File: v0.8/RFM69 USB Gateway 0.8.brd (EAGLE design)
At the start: 40.7 x 17.3 mm, 25 parts, among them CN1 MINIB, IC3 MCP1703CB, U2 ATMEGA328P-MU, X1 16 MHz

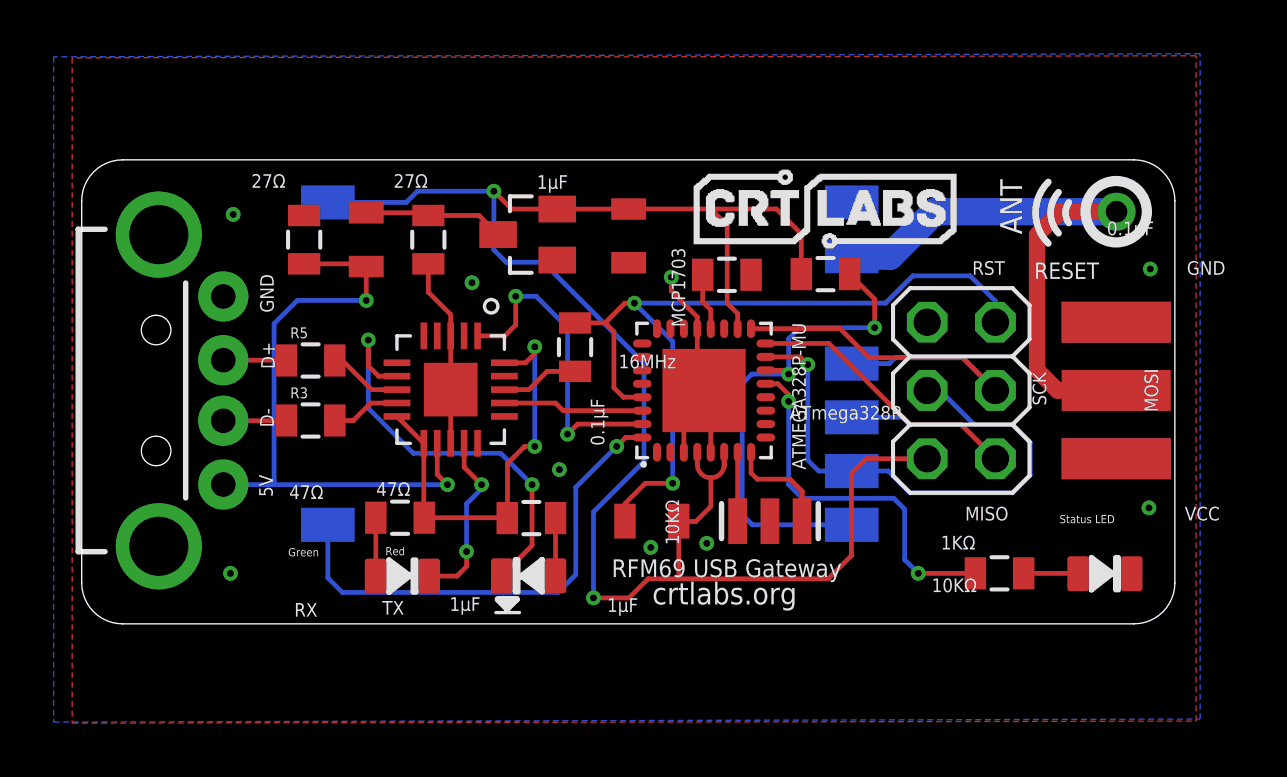
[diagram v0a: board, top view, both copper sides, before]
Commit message: Unsmashed and updated all component values
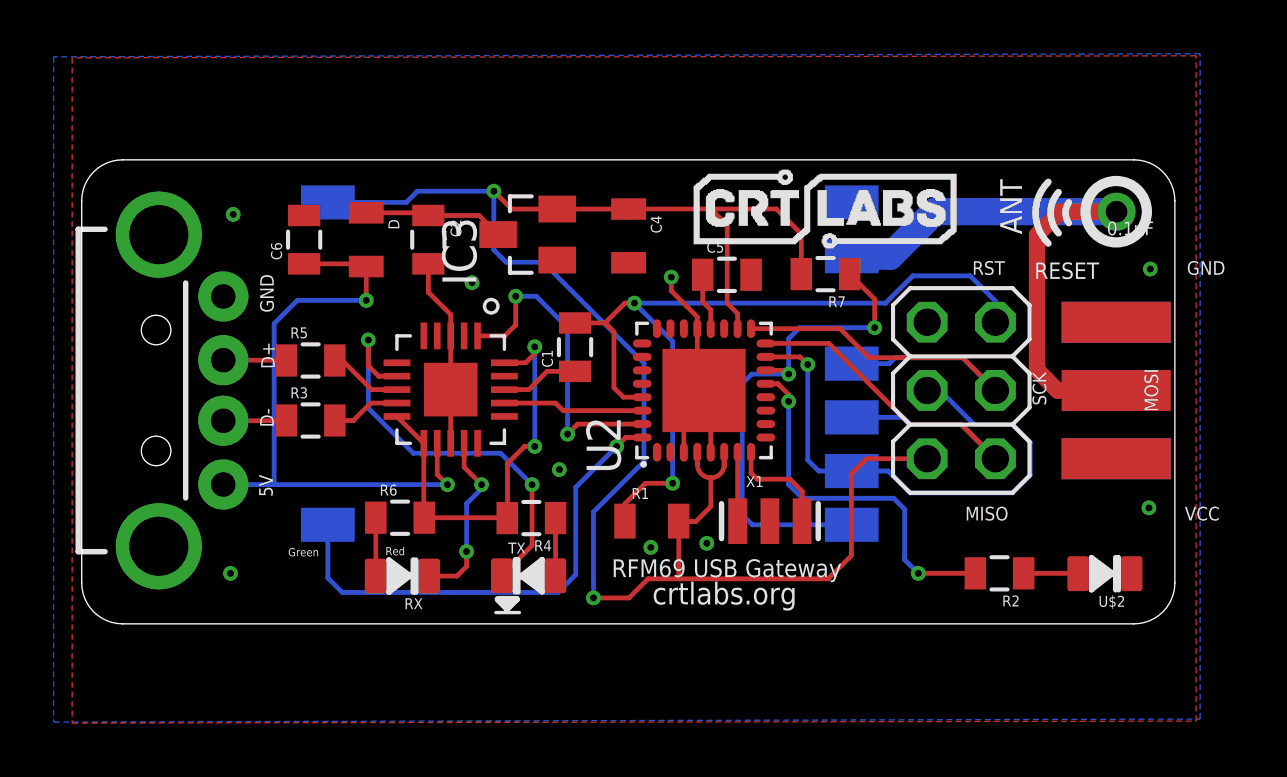
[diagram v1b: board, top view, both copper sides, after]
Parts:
- C1, C5: value 0.1 -> 0.1μF
- C2, C4: value 1u -> 1μF
- C6: value 0.1u -> 0.1μF
- R1: value 10k -> 10KΩ
- R2: value 1k -> 1KΩ
- R4, R6: value (none) -> 47Ω
- R7: value 10K -> 10KΩ
- RX: value LED0805 -> Green
- TX: value LED0805 -> Red
- renumbered U$4 to RX, U$7 to TX
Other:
- board text removed: "10KΩ"
- board text removed: "16MHz"
- board text removed: "1KΩ"
- board text removed: "1μF"
- board text removed: "27Ω"
- board text removed: "47Ω"
- board text removed: "ATmega328P"
- board text removed: "MCP1703"
- board text removed: "RX"
- board text removed: "Status LED"
- board text removed: "TX"
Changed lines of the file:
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@@
 <text x="51.6382" y="4.0894" size="1.016" layer="22" font="vector" ratio="15" rot="MR0">Akram Ali</text>
 <text x="13.462" y="11.5697" size="0.8128" layer="22" font="vector" ratio="9" rot="MR270" align="bottom-center">v0.8    2016</text>
-<text x="18.4023" y="19.1262" size="0.508" layer="121" font="vector">27Ω</text>
-<text x="23.6982" y="19.1262" size="0.508" layer="121" font="vector">27Ω</text>
-<text x="19.812" y="7.5438" size="0.508" layer="121" font="vector">47Ω</text>
-<text x="23.0505" y="7.6581" size="0.508" layer="121" font="vector">47Ω</text>
-<text x="34.3281" y="5.8293" size="0.508" layer="121" font="vector" rot="R90">10KΩ</text>
-<text x="44.069" y="5.6642" size="0.508" layer="121" font="vector">1KΩ</text>
-<text x="26.9367" y="3.8862" size="0.508" layer="121" font="vector" rot="R180">1μF</text>
-<text x="32.8041" y="3.8481" size="0.508" layer="121" font="vector" rot="R180">1μF</text>
 <text x="52.0065" y="17.8689" size="0.508" layer="121" font="vector" rot="R180">0.1μF</text>
-<text x="29.0322" y="19.0881" size="0.508" layer="121" font="vector">1μF</text>
-<text x="20.0025" y="3.1623" size="0.508" layer="121" font="vector">RX</text>
-<text x="23.2791" y="3.2385" size="0.508" layer="121" font="vector">TX</text>
 <text x="19.7739" y="5.4102" size="0.3048" layer="121" font="vector">Green</text>
 <text x="23.3934" y="5.4483" size="0.3048" layer="121" font="vector">Red</text>
-<text x="34.2138" y="12.9159" size="0.508" layer="121" font="vector" rot="R180">16MHz</text>
-<text x="34.5567" y="13.9446" size="0.508" layer="121" font="vector" rot="R90">MCP1703</text>
-<text x="48.4886" y="6.6421" size="0.3048" layer="121" font="vector">Status LED</text>
 <text x="19.2405" y="14.478" size="0.508" layer="121" font="vector" rot="R90">GND</text>
 <text x="19.2786" y="12.3825" size="0.508" layer="121" font="vector" rot="R90">D+</text>
@@
 <text x="31.8135" y="4.6355" size="0.6604" layer="21" font="vector" ratio="7">RFM69 USB Gateway</text>
 <text x="33.3248" y="3.6195" size="0.8128" layer="21" font="vector" ratio="12">crtlabs.org</text>
-<text x="43.7261" y="4.0767" size="0.508" layer="121" font="vector">10KΩ</text>
 <text x="46.2788" y="19.4437" size="0.8128" layer="21" font="vector" rot="R270">ANT</text>
-<text x="42.5958" y="11.0109" size="0.508" layer="121" font="vector" rot="R180">ATmega328P</text>
-<text x="31.5468" y="9.525" size="0.508" layer="121" font="vector" rot="R90">0.1μF</text>
 <rectangle x1="39.78275" y1="16.87195" x2="40.08755" y2="16.91005" layer="121"/>
 <rectangle x1="39.70655" y1="16.91005" x2="40.12565" y2="16.94815" layer="121"/>
@@
 </autorouter>
 <elements>
-<element name="X1" library="SparkFun" package="RESONATOR-SMD" value="16 MHz" x="37.7063" y="6.7183" smashed="yes"/>
-<element name="IC3" library="linear" package="SOT23" value="MCP1703CB" x="28.6893" y="17.3863" smashed="yes" rot="R90"/>
-<element name="C5" library="SparkFun" package="0805" value="0.1" x="36.1061" y="15.8877" smashed="yes"/>
-<element name="R1" library="LowPowerLab" package="0805" value="10k" x="33.3121" y="6.7183" smashed="yes"/>
-<element name="C4" library="LowPowerLab" package="0805" value="1u" x="32.4485" y="17.3355" smashed="yes" rot="R270"/>
-<element name="C2" library="SparkFun" package="0805" value="1u" x="24.9936" y="17.1958" smashed="yes" rot="R270"/>
-<element name="U$2" library="LowPowerLab" package="0805-LED" value="LED0805" x="50.1777" y="4.7625" smashed="yes" rot="R180"/>
-<element name="R2" library="SparkFun" package="0805" value="1k" x="46.2534" y="4.7752" smashed="yes" rot="R180"/>
+<element name="X1" library="SparkFun" package="RESONATOR-SMD" value="16 MHz" x="37.7063" y="6.7183"/>
+<element name="IC3" library="linear" package="SOT23" value="MCP1703CB" x="28.6893" y="17.3863" rot="R90"/>
+<element name="C5" library="SparkFun" package="0805" value="0.1μF" x="36.1061" y="15.8877"/>
+<element name="R1" library="LowPowerLab" package="0805" value="10KΩ" x="33.3121" y="6.7183"/>
+<element name="C4" library="LowPowerLab" package="0805" value="1μF" x="32.4485" y="17.3355" rot="R270"/>
+<element name="C2" library="SparkFun" package="0805" value="1μF" x="24.9936" y="17.1958" rot="R270"/>
+<element name="U$2" library="LowPowerLab" package="0805-LED" value="LED0805" x="50.1777" y="4.7625" rot="R180"/>
+<element name="R2" library="SparkFun" package="0805" value="1KΩ" x="46.2534" y="4.7752" rot="R180"/>
 <element name="U$1" library="LowPowerLab" package="RFM12B-ANTENNA" value="RFM12B_ANTENNA" x="50.6095" y="18.2372"/>
 <element name="U$5" library="LowPowerLab" package="RFM69W-MINPADS" value="RFM69" x="32.7533" y="11.5824" smashed="yes" rot="MR180"/>
@@
 <attribute name="PROD_ID" value="CONN-08367" x="14.9606" y="11.5824" size="1.778" layer="27" display="off"/>
 </element>
-<element name="R4" library="SparkFun" package="0805" value="" x="28.829" y="6.8326" smashed="yes" rot="R180">
-<attribute name="VALUE" x="29.845" y="7.9756" size="0.4064" layer="27" font="vector" rot="R180"/>
-</element>
-<element name="R6" library="SparkFun" package="0805" value="" x="23.9395" y="6.8453" smashed="yes">
-<attribute name="VALUE" x="22.9235" y="5.7023" size="0.4064" layer="27" font="vector"/>
-</element>
-<element name="U$4" library="LowPowerLab" package="0805-LED" value="LED0805" x="24.0284" y="4.6736" smashed="yes" rot="R180"/>
-<element name="U$7" library="LowPowerLab" package="0805-LED" value="LED0805" x="28.7274" y="4.6863" smashed="yes"/>
-<element name="C6" library="SparkFun" package="0805" value="0.1u" x="20.3708" y="17.1958" smashed="yes" rot="R90"/>
-<element name="D" library="LowPowerLab" package="0805" value="SHOTTKY" x="22.6822" y="17.1958" smashed="yes" rot="R270"/>
+<element name="R4" library="SparkFun" package="0805" value="47Ω" x="28.829" y="6.8326" rot="R180"/>
+<element name="R6" library="SparkFun" package="0805" value="47Ω" x="23.9395" y="6.8453"/>
+<element name="RX" library="LowPowerLab" package="0805-LED" value="Green" x="24.0284" y="4.6736" rot="R180"/>
+<element name="TX" library="LowPowerLab" package="0805-LED" value="Red" x="28.7274" y="4.6863"/>
+<element name="C6" library="SparkFun" package="0805" value="0.1μF" x="20.3708" y="17.1958" rot="R90"/>
+<element name="D" library="LowPowerLab" package="0805" value="SHOTTKY" x="22.6822" y="17.1958" rot="R270"/>
 <element name="R3" library="SparkFun" package="0805" value="27Ω" x="20.6121" y="10.4648"/>
 <element name="R5" library="SparkFun" package="0805" value="27Ω" x="20.6121" y="12.7"/>
@@
 <attribute name="VALUE" x="49.276" y="7.7724" size="1.27" layer="27" rot="R90"/>
 </element>
-<element name="R7" library="SparkFun" package="0805" value="10K" x="39.7764" y="15.9131" smashed="yes" rot="R180"/>
-<element name="C1" library="SparkFun" package="0805" value="0.1" x="30.4546" y="13.1953" smashed="yes" rot="R90"/>
+<element name="R7" library="SparkFun" package="0805" value="10KΩ" x="39.7764" y="15.9131" rot="R180"/>
+<element name="C1" library="SparkFun" package="0805" value="0.1μF" x="30.4546" y="13.1953" rot="R90"/>
 <element name="J$1" library="SparkFun-Connectors" package="SMA-EDGE" value="SMA_EDGE" x="50.5968" y="9.0424" rot="R90"/>
-<element name="U2" library="ATMEGA328P-MU" package="QFN50P500X500X100-33N" value="ATMEGA328P-MU" x="35.2552" y="11.5824" smashed="yes" rot="R90">
+<element name="U2" library="ATMEGA328P-MU" package="QFN50P500X500X100-33N" value="ATMEGA328P-MU" x="35.2552" y="11.5824" rot="R90">
 <attribute name="AVAILABILITY" value="Good" x="35.2552" y="11.5824" size="1.778" layer="27" rot="R90" display="off"/>
 <attribute name="MP" value="ATMEGA328P-MU" x="35.2552" y="11.5824" size="1.778" layer="27" rot="R90" display="off"/>
@@
 <attribute name="MF" value="Atmel" x="35.2552" y="11.5824" size="1.778" layer="27" rot="R90" display="off"/>
 <attribute name="PRICE" value="2.55 USD" x="35.2552" y="11.5824" size="1.778" layer="27" rot="R90" display="off"/>
-<attribute name="VALUE" x="39.043709375" y="8.635590625" size="0.508" layer="121" font="vector" rot="R90"/>
 </element>
 <element name="FT231XQ-R" library="ftdi_ft231xq-r" package="FTDI_FT231XQ-R_PACKAGE" value="FT231XQ-R" x="25.8572" y="11.5824" rot="R270"/>
@@
 </signal>
 <signal name="N$6">
-<contactref element="U$4" pad="MINUS"/>
+<contactref element="RX" pad="MINUS"/>
 <contactref element="FT231XQ-R" pad="CBUS1"/>
 <wire x1="26.3252" y1="9.6144" x2="26.3252" y2="8.7268" width="0.1778" layer="1"/>
@@
 </signal>
 <signal name="N$7">
-<contactref element="U$7" pad="MINUS"/>
+<contactref element="TX" pad="MINUS"/>
 <contactref element="FT231XQ-R" pad="CBUS2"/>
 <wire x1="23.8252" y1="12.1144" x2="23.1408" y2="12.1144" width="0.1778" layer="1"/>
@@
 <signal name="N$8">
 <contactref element="R4" pad="1"/>
-<contactref element="U$7" pad="PLUS"/>
+<contactref element="TX" pad="PLUS"/>
 <wire x1="29.7274" y1="4.6863" x2="29.7274" y2="6.831" width="0.1778" layer="1"/>
 <wire x1="29.7274" y1="6.831" x2="29.729" y2="6.8326" width="0.1778" layer="1"/>
 </signal>
 <signal name="N$9">
-<contactref element="U$4" pad="PLUS"/>
+<contactref element="RX" pad="PLUS"/>
 <contactref element="R6" pad="1"/>
 <wire x1="23.0395" y1="6.8453" x2="23.0395" y2="4.6847" width="0.1778" layer="1"/>

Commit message: Fixed silkscreen
Changed all fonts to vector; silkscreen now on layer 121, adjusted some
components and traces
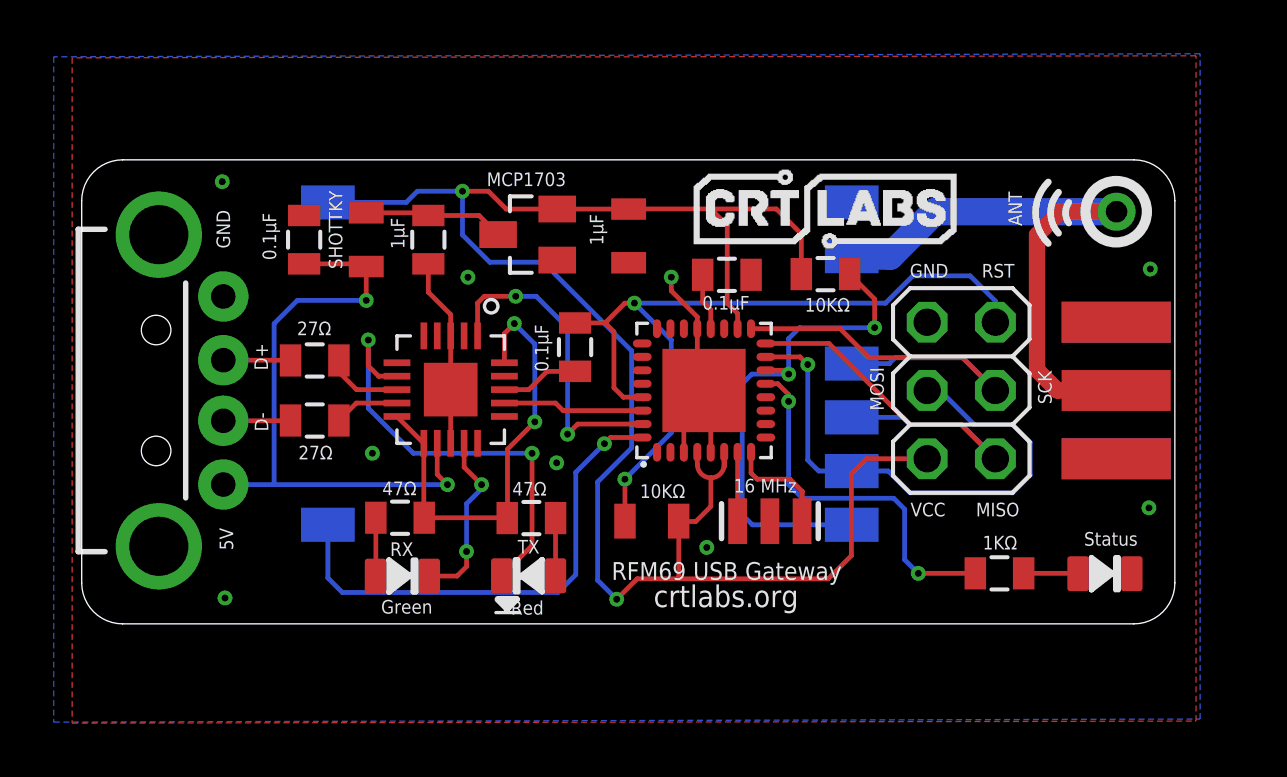
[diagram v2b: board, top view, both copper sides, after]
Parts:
- IC3: value MCP1703CB -> MCP1703
- U$2: value LED0805 -> Status
- moved R3 0.15 mm to (20.8, 10.5)
- moved R5 0.15 mm to (20.8, 12.7)
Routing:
- net FTDI3.3V: track 15.8 -> 16.9 mm
- net N$7: track 15.9 -> 16.5 mm
- net RESET: track 31.3 -> 30.7 mm
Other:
- board text removed: "0.1μF"
- board text removed: "Green"
- board text removed: "RESET"
- board text removed: "Red"
